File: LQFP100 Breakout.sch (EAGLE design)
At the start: 9 parts, among them U1 LPC2368

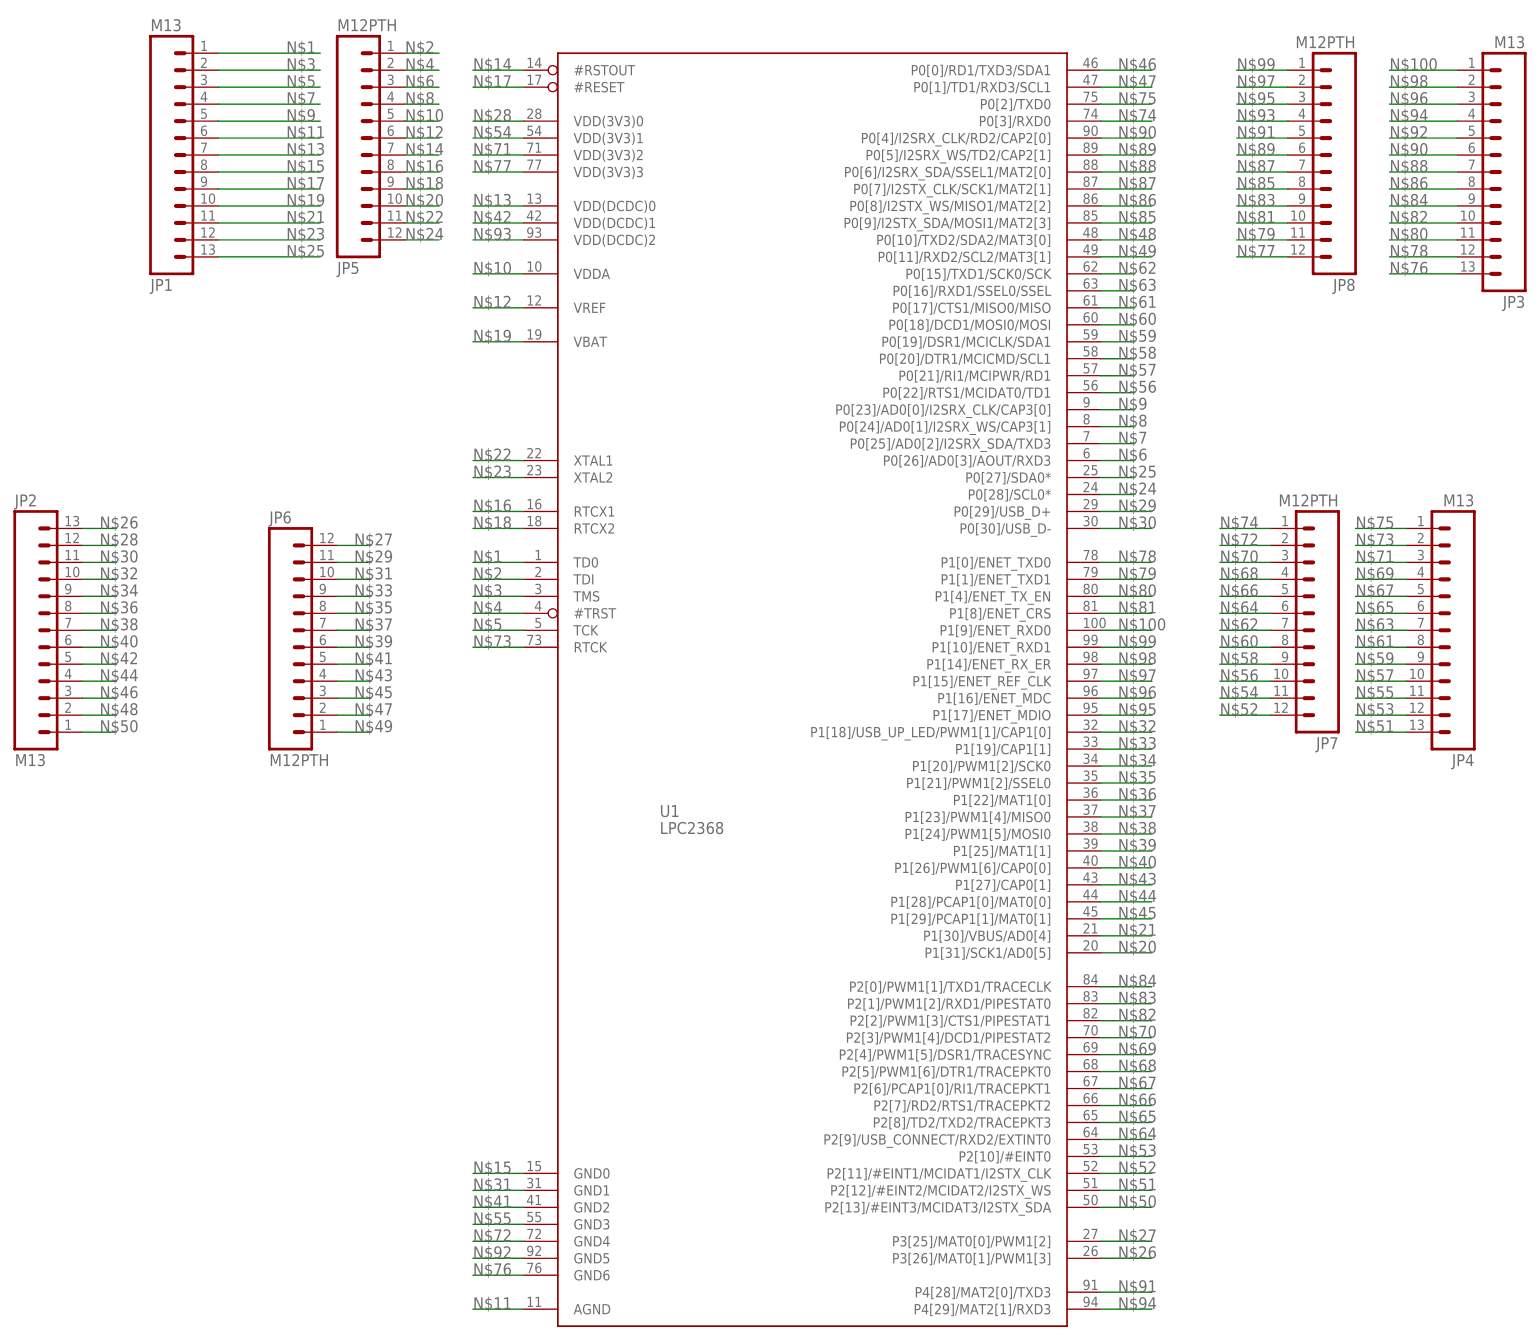
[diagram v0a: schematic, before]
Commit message: Merged Mio's KwanSystems.lbr, updated all eagle files to use it.
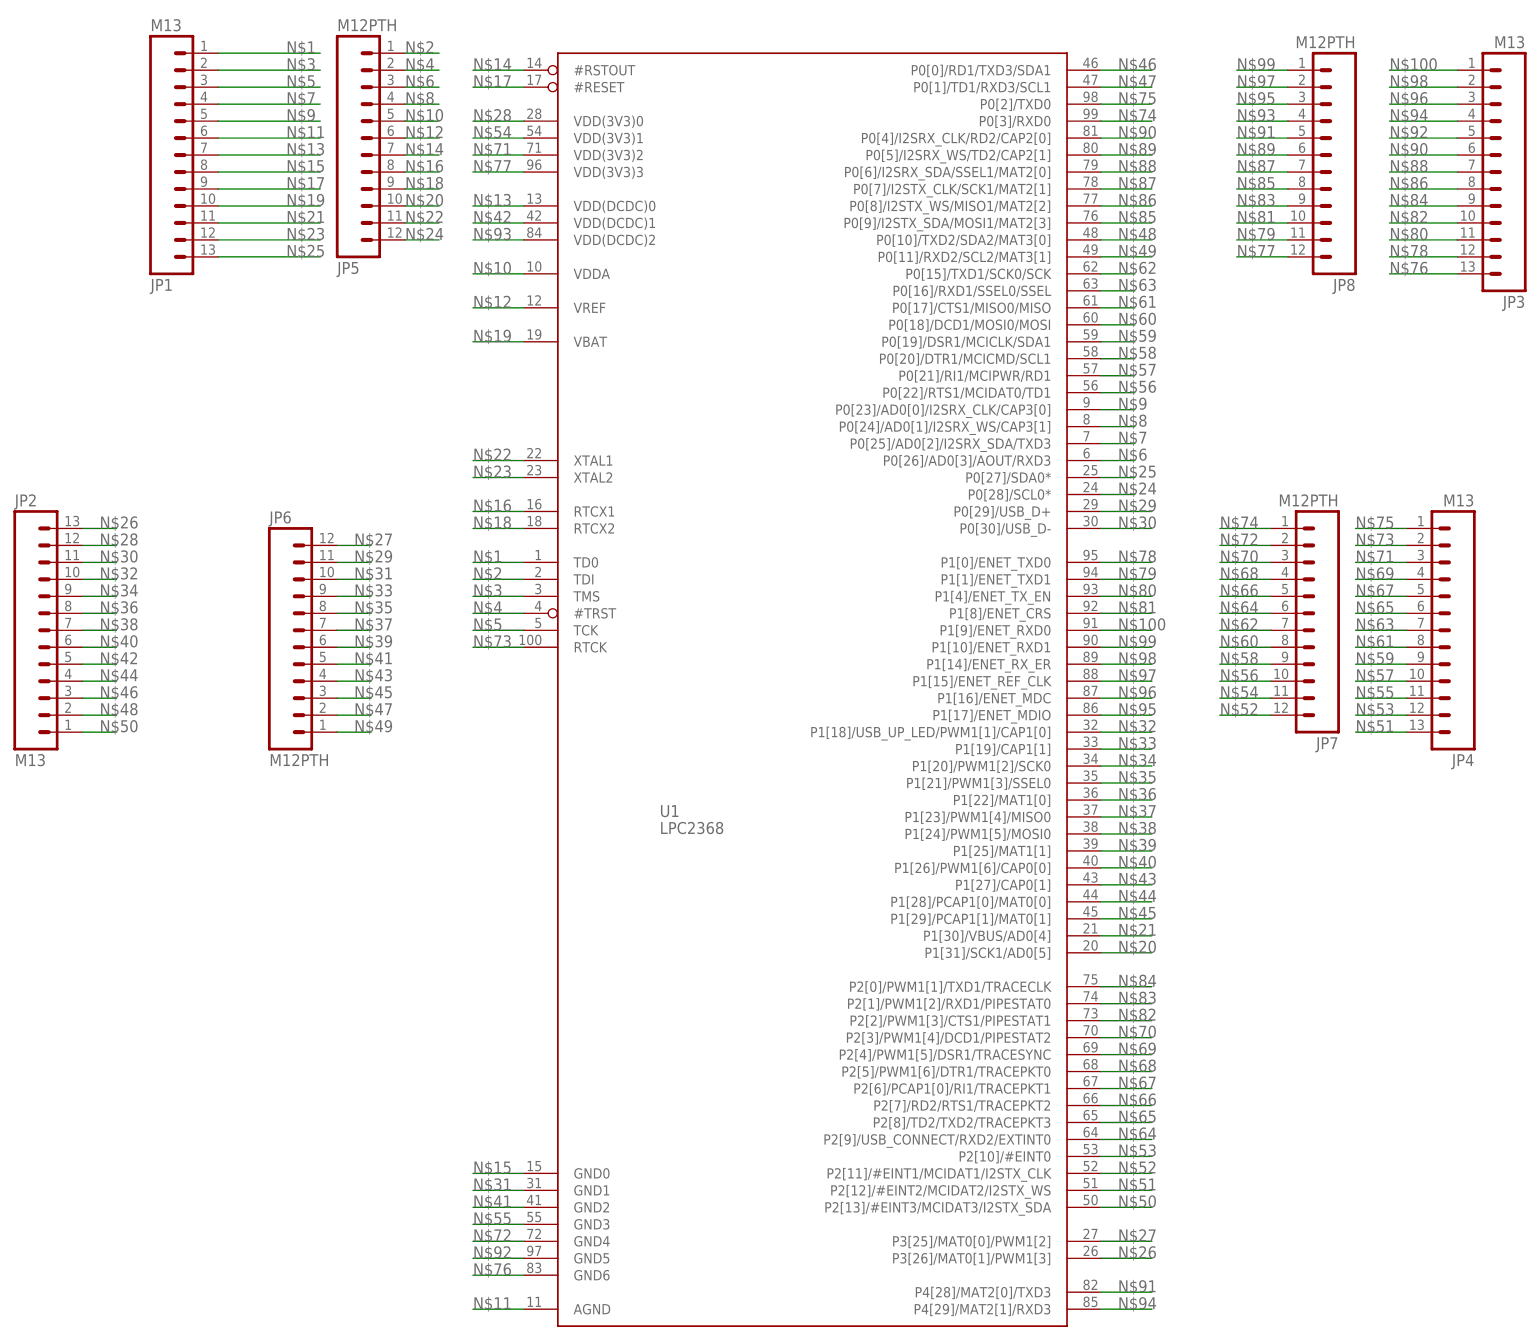
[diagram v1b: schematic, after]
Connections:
- net N$35: now also U1.P1[21]/PWM1[3]/SSEL0; no longer U1.P1[21]/PWM1[2]/SSEL0
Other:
- moved on the sheet: U1
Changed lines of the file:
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@@
 <?xml version="1.0" encoding="utf-8"?>
 <!DOCTYPE eagle SYSTEM "eagle.dtd">
-<eagle version="6.1">
+<eagle version="6.2">
 <drawing>
 <settings>
@@
 </segment>
 <segment>
-<pinref part="U1" gate="G$1" pin="P1[21]/PWM1[2]/SSEL0"/>
+<pinref part="U1" gate="G$1" pin="P1[21]/PWM1[3]/SSEL0"/>
 <wire x1="119.38" y1="-17.78" x2="127" y2="-17.78" width="0.1524" layer="91"/>
 <label x="121.92" y="-17.78" size="1.778" layer="95"/>
